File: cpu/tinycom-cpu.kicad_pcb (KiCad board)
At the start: 4 copper layers, 39.9 x 41.4 mm, 10 parts, among them P1 CONN_02X08, P2 CONN_02X08, U1 OLIMEX_IC_A13, U2 H5TQG63BFR/FBGA96, Y1 Crystal

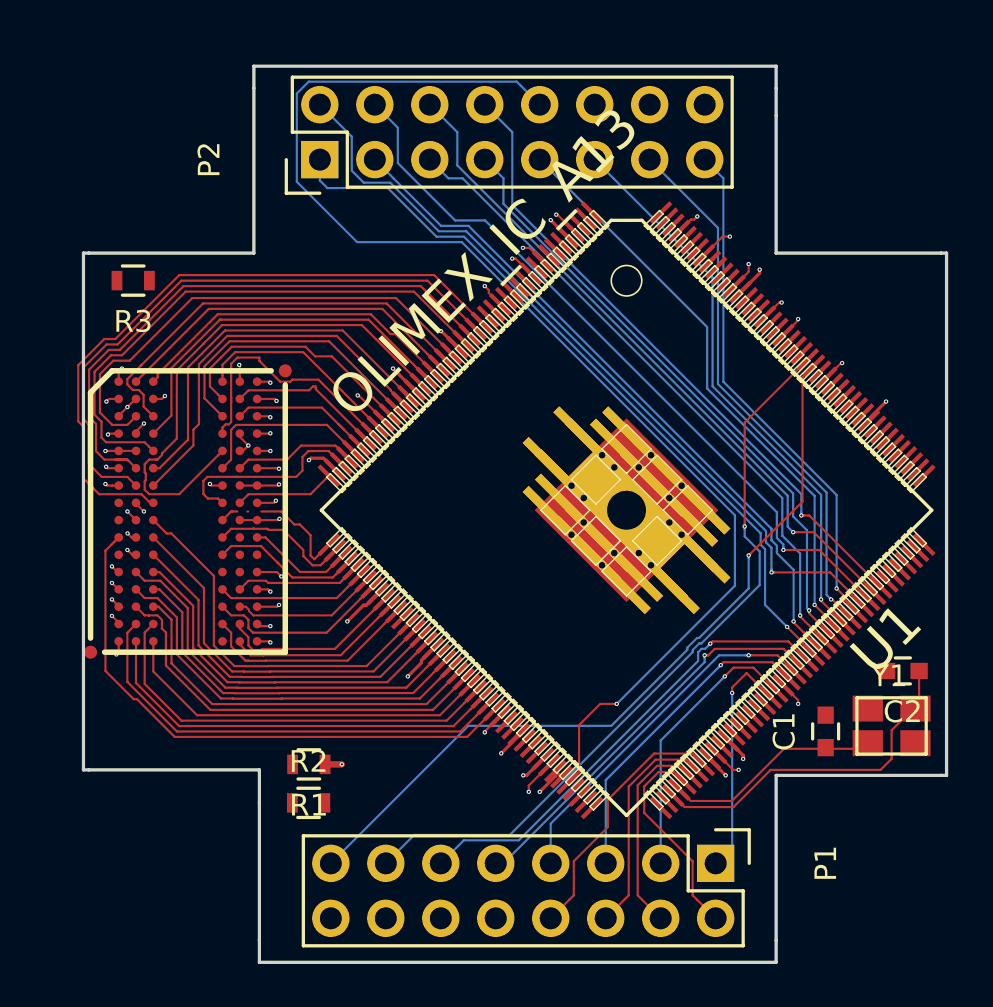
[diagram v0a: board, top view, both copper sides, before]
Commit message: change ddr to bga78
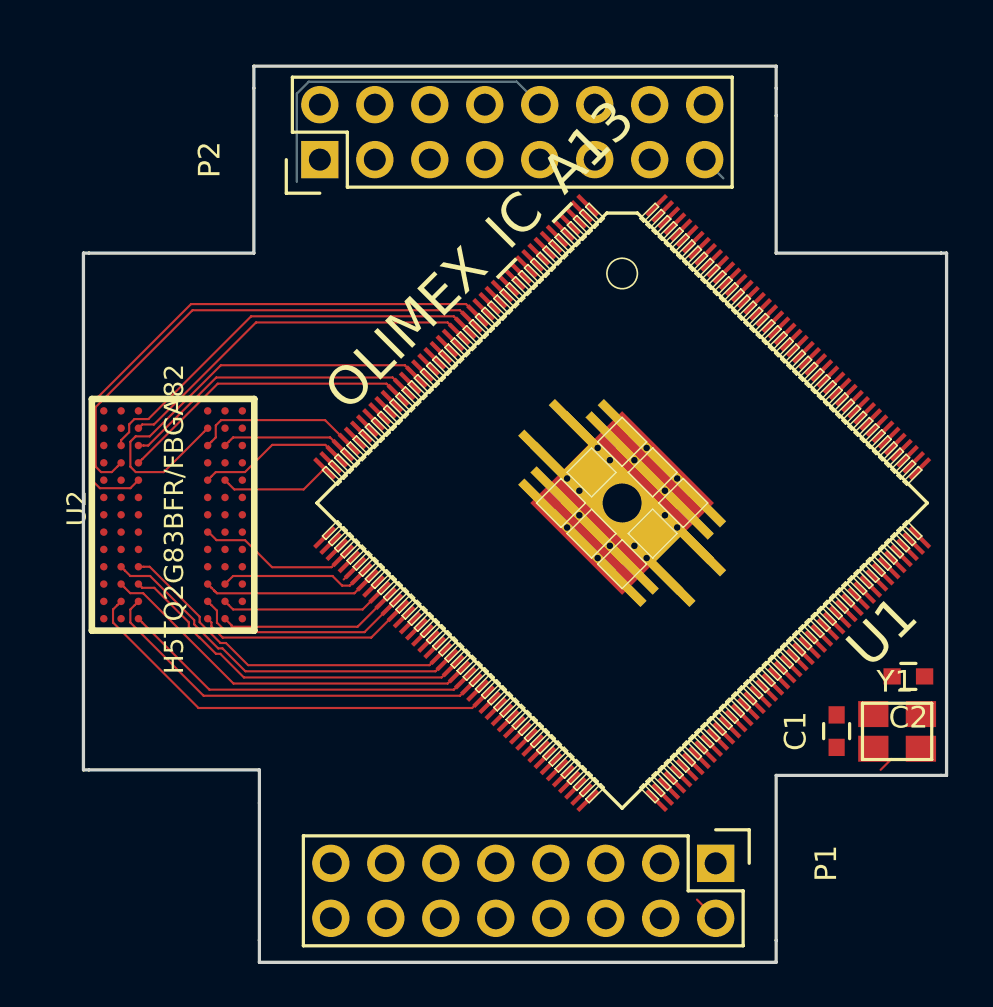
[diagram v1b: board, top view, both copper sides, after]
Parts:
- removed R1, R2, R3: R, Resistors_SMD:R_0603
- U1: footprint allwinner_a13-OLIMEX_IC_TQFP176 -> A13o:allwinner_a13-OLIMEX_IC_TQFP176
- U2: value H5TQG63BFR/FBGA96 -> H5TQ2G83BFR/FBGA82; footprint ax209:ax209-OLIMEX_IC_FBGA96 -> BGA78:BGA78
- moved U2 6.06 mm to (79.4, 106.3)
- moved C1 0.51 mm to (113.3, 121.1)
- moved U1 0.39 mm to (103.4, 110.6)
- moved Y1 0.36 mm to (116.1, 121.2)
- moved C2 0.36 mm to (116.6, 118.6)
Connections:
- U1 pad 19: DDR_D4 -> DDR3_D4
- U1 pad 20: DDR_D6 -> DDR3_D6
- U1 pad 21: DDR_D2 -> DDR3_D2
- U1 pad 22: DDR_D0 -> DDR3_D0
- U1 pad 24: DDR_D11 -> DDR3_D11
- U1 pad 25: DDR_D9 -> DDR3_D9
- U1 pad 26: DDR_D13 -> DDR3_D13
- U1 pad 27: DDR_D15 -> DDR3_D15
- U1 pad 28: DDR_DQM1 -> DDR3_DM1
- U1 pad 29: DDR_DQM0 -> DDR3_DM0
- U1 pad 31: DDR_DQS0_P -> DDR3_DQS0_P
- U1 pad 32: DDR_DQS0_N -> DDR3_DQS0_N
- U1 pad 33: DDR_DQS1_P -> DDR3_DQS1_P
- U1 pad 34: DDR_DQS1_N -> DDR3_DQS1_N
- U1 pad 36: DDR_D12 -> DDR3_D12
- U1 pad 37: DDR_D8 -> DDR3_D8
- U1 pad 38: DDR_D14 -> DDR3_D14
- U1 pad 39: DDR_D10 -> DDR3_D10
- U1 pad 40: DDR_D1 -> DDR3_D1
- U1 pad 41: DDR_D3 -> DDR3_D3
- U1 pad 42: DDR_D7 -> DDR3_D7
- U1 pad 44: DDR_D5 -> DDR3_D5
- U1 pad 48: DDR_A10 -> DDR3_A10
- U1 pad 50: DDR_A12 -> DDR3_A12
- U1 pad 51: DDR_A4 -> DDR3_A4
- U1 pad 52: DDR_A1 -> DDR3_A1
- U1 pad 54: DDR_A6 -> DDR3_A6
- U1 pad 55: DDR_A8 -> DDR3_A8
- U1 pad 56: DDR_A11 -> DDR3_A11
- U1 pad 57: DDR_A14 -> DDR3_A14
- U1 pad 64: DDR_A0 -> DDR3_A0
- U1 pad 65: DDR_A3 -> DDR3_A3
- U1 pad 66: DDR_A2 -> DDR3_A2
- U1 pad 67: DDR_A5 -> DDR3_A5
- U1 pad 68: DDR_A13 -> DDR3_A13
- U1 pad 69: DDR_A9 -> DDR3_A9
- U1 pad 71: DDR_A7 -> DDR3_A7
- U1 pad 72: DDR_ODT -> DDR3_ODT
- U2 pad A1: VCC_15 -> Net-(U2-PadA1)
- U2 pad A2: DDR_D13 -> Net-(U2-PadA2)
- U2 pad A3: DDR_D15 -> Net-(U2-PadA3)
- U2 pad A7: DDR_D12 -> Net-(U2-PadA7)
- U2 pad A8: VCC_15 -> Net-(U2-PadA8)
- U2 pad A9: GND -> Net-(U2-PadA9)
- U2 pad B1: GND -> Net-(U2-PadB1)
- U2 pad B2: VCC_15 -> Net-(U2-PadB2)
- U2 pad B3: GND -> DDR3_D0
- U2 pad B7: DDR_DQS1_N -> DDR3_DM0
- U2 pad B8: DDR_D14 -> Net-(U2-PadB8)
- U2 pad B9: GND -> Net-(U2-PadB9)
- U2 pad C1: VCC_15 -> Net-(U2-PadC1)
- U2 pad C2: DDR_D11 -> DDR3_D2
- U2 pad C3: DDR_D9 -> DDR3_DQS0_P
- U2 pad C7: DDR_DQS1_P -> DDR3_D1
- U2 pad C8: DDR_D10 -> DDR3_D3
- U2 pad C9: VCC_15 -> Net-(U2-PadC9)
- U2 pad D1: GND -> Net-(U2-PadD1)
- U2 pad D2: VCC_15 -> DDR3_D6
- U2 pad D3: DDR_DQM1 -> DDR3_DQS0_N
- U2 pad D7: DDR_D8 -> Net-(U2-PadD7)
- U2 pad D8: GND -> Net-(U2-PadD8)
- U2 pad D9: VCC_15 -> Net-(U2-PadD9)
- U2 pad E1: GND -> Net-(U2-PadE1)
- U2 pad E2: GND -> Net-(U2-PadE2)
- U2 pad E3: DDR_D0 -> DDR3_D4
- U2 pad E7: DDR_DQM0 -> DDR3_D7
- U2 pad E8: GND -> DDR3_D5
- U2 pad E9: VCC_15 -> Net-(U2-PadE9)
- U2 pad F1: VCC_15 -> Net-(U2-PadF1)
- U2 pad F2: DDR_D2 -> Net-(U2-PadF2)
- U2 pad F3: DDR_DQS0_P -> Net-(U2-PadF3)
- U2 pad F7: DDR_D1 -> Net-(U2-PadF7)
- U2 pad F8: DDR_D3 -> Net-(U2-PadF8)
- U2 pad F9: GND -> Net-(U2-PadF9)
- U2 pad G1: GND -> Net-(U2-PadG1)
- U2 pad G2: DDR_D6 -> Net-(U2-PadG2)
- U2 pad G3: DDR_DQS0_N -> Net-(U2-PadG3)
- U2 pad G7: VCC_15 -> Net-(U2-PadG7)
- U2 pad G8: GND -> Net-(U2-PadG8)
- U2 pad G9: GND -> Net-(U2-PadG9)
- U2 pad H1: Net-(R1-Pad2) -> Net-(U2-PadH1)
- U2 pad H2: VCC_15 -> Net-(U2-PadH2)
- U2 pad H3: DDR_D4 -> Net-(U2-PadH3)
- U2 pad H7: DDR_D7 -> DDR3_A10
- U2 pad H8: DDR_D5 -> Net-(U2-PadH8)
- U2 pad H9: VCC_15 -> Net-(U2-PadH9)
- U2 pad J2: GND -> Net-(U2-PadJ2)
- U2 pad J3: DDR_RAS_N -> Net-(U2-PadJ3)
- U2 pad J7: DDR_CK_P -> Net-(U2-PadJ7)
- U2 pad J8: GND -> Net-(U2-PadJ8)
- U2 pad J9: GND -> Net-(U2-PadJ9)
- U2 pad K1: DDR_ODT -> Net-(U2-PadK1)
- U2 pad K2: VCC_15 -> DDR3_A3
- U2 pad K3: DDR_CAS_N -> DDR3_A0
- U2 pad K7: DDR_CK_N -> DDR3_A12
- U2 pad K8: VCC_15 -> Net-(U2-PadK8)
- U2 pad K9: DDR_CKE -> Net-(U2-PadK9)
- U2 pad L2: GND -> DDR3_A5
- U2 pad L3: DDR_WE_N -> DDR3_A2
- U2 pad L7: DDR_A10 -> DDR3_A1
- U2 pad L8: Net-(R3-Pad1) -> DDR3_A4
- U2 pad M1: GND -> Net-(U2-PadM1)
- U2 pad M2: DDR_BA0 -> DDR3_A7
- U2 pad M3: DDR_BA2 -> DDR3_A9
- U2 pad M7: Net-(U2-PadM7) -> DDR3_A11
- U2 pad M8: Net-(R1-Pad2) -> DDR3_A6
- U2 pad M9: GND -> Net-(U2-PadM9)
- U2 pad N1: VCC_15 -> Net-(U2-PadN1)
- U2 pad N2: DDR_A3 -> Net-(U2-PadN2)
- U2 pad N3: DDR_A0 -> DDR3_A13
- U2 pad N7: DDR_A12 -> DDR3_A14
- U2 pad N8: DDR_BA1 -> DDR3_A8
- U2 pad N9: VCC_15 -> Net-(U2-PadN9)
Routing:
- net VCC_15: track 63.7 -> 0.00 mm, vias 22 -> 0
- net MICIN1: track 58.6 -> 16.0 mm, vias 1 -> 0
- net CSI_D4: track 36.6 -> 0.00 mm, vias 1 -> 0
- net UART1_RX: track 36.2 -> 0.00 mm, vias 1 -> 0
- net CSI_CLK: track 34.7 -> 0.00 mm, vias 1 -> 0
- net UART1_TX: track 34.6 -> 0.00 mm, vias 1 -> 0
- net CSI_D5: track 34.1 -> 0.00 mm, vias 1 -> 0
- net CSI_MCLK: track 31.9 -> 0.00 mm, vias 1 -> 0
- net CSI_D6: track 31.7 -> 0.00 mm, vias 1 -> 0
- net DDR_D4: track 30.5 -> 0.00 mm
- net CSI_HSYNC: track 30.3 -> 0.00 mm, vias 1 -> 0
- net CSI_D7: track 30.1 -> 0.00 mm, vias 1 -> 0
- net CSI_VSYNC: track 28.7 -> 0.00 mm, vias 1 -> 0
- net DDR_D6: track 27.9 -> 0.00 mm
- net CSI_D0: track 27.5 -> 0.00 mm, vias 1 -> 0
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
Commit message: route new ddr
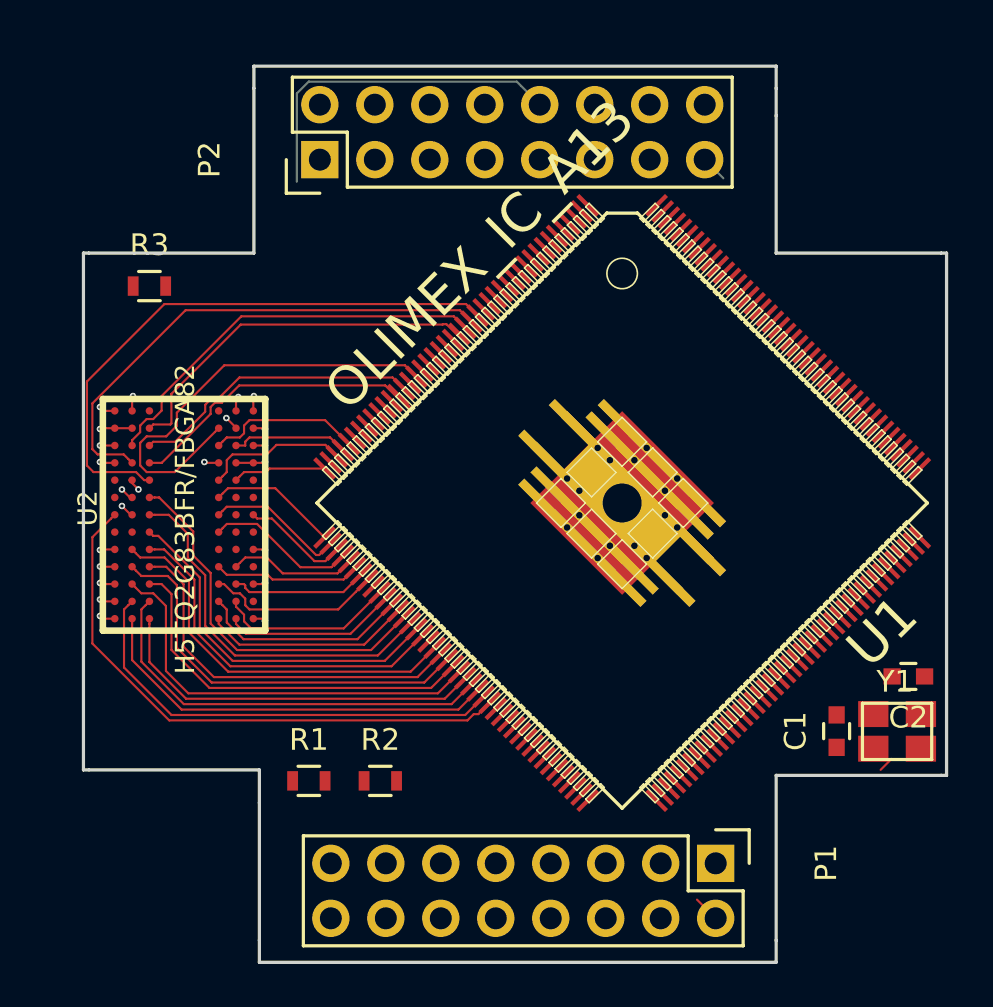
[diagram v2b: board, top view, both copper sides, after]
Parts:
- added R1: R, Resistors_SMD:R_0603, F.Cu at (88.9, 123.4)
- added R2: R, Resistors_SMD:R_0603, F.Cu at (92.2, 123.4)
- added R3: R, Resistors_SMD:R_0603, F.Cu at (81.5, 100.6)
- moved U2 0.51 mm to (79.9, 106.3)
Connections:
- U1 pad 45: DDR_CK_P -> DDR3_CK_P
- U1 pad 46: DDR_CK_N -> DDR3_CK_N
- U1 pad 47: DDR_CKE -> DDR3_CKE
- U1 pad 49: DDR_BA1 -> DDR3_BA1
- U1 pad 58: DDR_RAS_N -> DDR3_RAS_N
- U1 pad 59: DDR_CAS_N -> DDR3_CAS_N
- U1 pad 60: DDR_WE_N -> DDR3_WE_N
- U1 pad 61: DDR_BA2 -> DDR3_BA2
- U1 pad 63: DDR_BA0 -> DDR3_BA0
- U1 pad 70: DDR_RST -> DDR3_RST
- U2 pad A1: Net-(U2-PadA1) -> GND
- U2 pad A2: Net-(U2-PadA2) -> VCC_15
- U2 pad A8: Net-(U2-PadA8) -> GND
- U2 pad A9: Net-(U2-PadA9) -> VCC_15
- U2 pad B1: Net-(U2-PadB1) -> GND
- U2 pad B2: Net-(U2-PadB2) -> GND
- U2 pad B8: Net-(U2-PadB8) -> GND
- U2 pad B9: Net-(U2-PadB9) -> VCC_15
- U2 pad C1: Net-(U2-PadC1) -> VCC_15
- U2 pad C9: Net-(U2-PadC9) -> GND
- U2 pad D1: Net-(U2-PadD1) -> GND
- U2 pad D7: Net-(U2-PadD7) -> VCC_15
- U2 pad D8: Net-(U2-PadD8) -> GND
- U2 pad D9: Net-(U2-PadD9) -> GND
- U2 pad E1: Net-(U2-PadE1) -> Net-(R1-Pad2)
- U2 pad E2: Net-(U2-PadE2) -> VCC_15
- U2 pad E9: Net-(U2-PadE9) -> VCC_15
- U2 pad F2: Net-(U2-PadF2) -> GND
- U2 pad F3: Net-(U2-PadF3) -> DDR3_RAS_N
- U2 pad F7: Net-(U2-PadF7) -> DDR3_CK_P
- U2 pad F8: Net-(U2-PadF8) -> GND
- U2 pad G1: Net-(U2-PadG1) -> DDR3_ODT
- U2 pad G2: Net-(U2-PadG2) -> VCC_15
- U2 pad G3: Net-(U2-PadG3) -> DDR3_CAS_N
- U2 pad G7: Net-(U2-PadG7) -> DDR3_CK_N
- U2 pad G8: Net-(U2-PadG8) -> VCC_15
- U2 pad G9: Net-(U2-PadG9) -> DDR3_CKE
- U2 pad H2: Net-(U2-PadH2) -> GND
- U2 pad H3: Net-(U2-PadH3) -> DDR3_WE_N
- U2 pad J1: Net-(U2-PadJ1) -> GND
- U2 pad J2: Net-(U2-PadJ2) -> DDR3_BA0
- U2 pad J3: Net-(U2-PadJ3) -> DDR3_BA2
- U2 pad J8: Net-(U2-PadJ8) -> Net-(R1-Pad2)
- U2 pad J9: Net-(U2-PadJ9) -> GND
- U2 pad K1: Net-(U2-PadK1) -> VCC_15
- U2 pad K8: Net-(U2-PadK8) -> DDR3_BA1
- U2 pad K9: Net-(U2-PadK9) -> VCC_15
- U2 pad L1: Net-(U2-PadL1) -> GND
- U2 pad L9: Net-(U2-PadL9) -> GND
- U2 pad M1: Net-(U2-PadM1) -> VCC_15
- U2 pad M9: Net-(U2-PadM9) -> VCC_15
- U2 pad N1: Net-(U2-PadN1) -> GND
- U2 pad N2: Net-(U2-PadN2) -> DDR3_RST
- U2 pad N9: Net-(U2-PadN9) -> GND
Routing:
- net DDR3_ODT: track 0.00 -> 26.5 mm
- net DDR3_RST: track 0.00 -> 19.2 mm
- net DDR3_BA0: track 0.00 -> 18.2 mm
- net DDR3_CAS_N: track 0.00 -> 17.4 mm
- net DDR3_RAS_N: track 0.00 -> 17.3 mm
- net DDR3_BA2: track 0.00 -> 16.8 mm
- net DDR3_WE_N: track 0.00 -> 16.8 mm
- net GND: track 0.00 -> 10.6 mm, vias 0 -> 14
- net DDR3_CK_N: track 0.00 -> 6.47 mm
- net VCC_15: track 0.00 -> 6.04 mm, vias 0 -> 9
- net DDR3_A12: track 0.75 -> 6.77 mm
- net DDR3_CK_P: track 0.00 -> 6.01 mm
- net DDR3_BA1: track 0.00 -> 5.92 mm
- net DDR3_CKE: track 0.00 -> 4.96 mm
- net DDR3_A5: track 17.7 -> 19.4 mm
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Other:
- net class Default: via_dia 0.2 -> 0.3; via_drill 0.1 -> 0.15
- net class ddr_address removed
- net class ddr_byte_0 removed
- net class ddr_byte_1 removed
- net class ddr_clock removed
- net class ddr_control removed
- net class vcc_15 removed
- net class vcc_33 removed

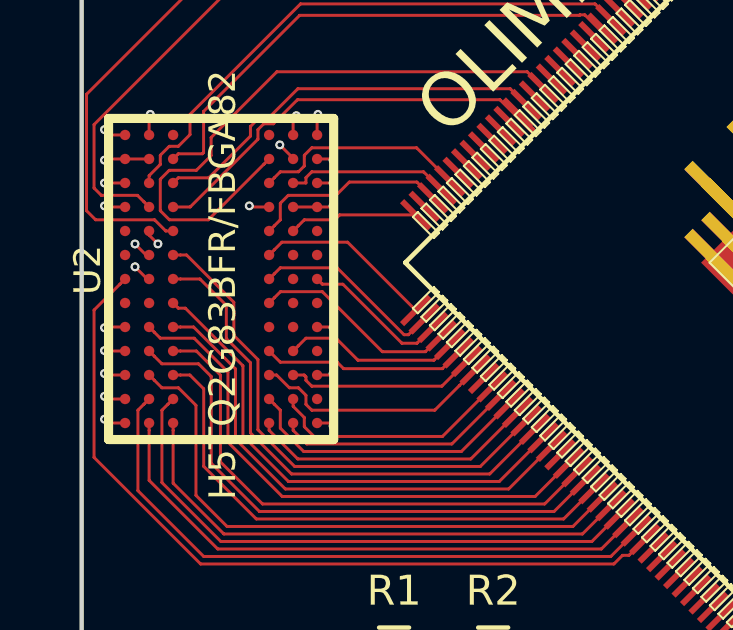
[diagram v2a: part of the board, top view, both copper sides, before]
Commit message: add ddr power plane
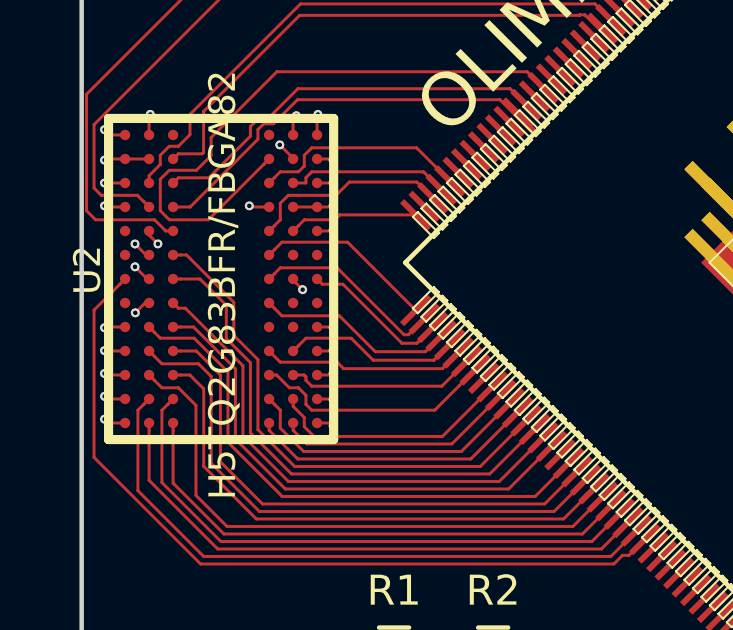
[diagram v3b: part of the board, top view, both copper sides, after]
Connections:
- P1 pad 12: VCC_15 -> VCC_33
- P1 pad 14: VCC_30 -> VCC_15
- P1 pad 16: VCC_33 -> GND
- P2 pad 14: GND -> VCC_30
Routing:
- net VCC_15: track 6.04 -> 76.7 mm, vias 9 -> 13
- net VCC_33: track 6.22 -> 0.00 mm
- net GND: track 10.6 -> 11.2 mm, vias 14 -> 15
- added copper zone on In2.Cu, net VCC_15

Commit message: router power
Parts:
- moved C2 4.38 mm to (113.0, 121.2), turned to 90 degrees
- moved C1 3.95 mm to (116.3, 118.6), turned to 180 degrees
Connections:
- P1 pad 1: SDC0_D1 -> SDC0_D2
- P1 pad 11: SDC0_D2 -> SDC0_D1
- P1 pad 13: UART1_TX -> UART1_RX
- P1 pad 15: UART1_RX -> UART1_TX
- P1 pad 3: SDC0_D0 -> SDC0_D3
- P1 pad 5: SDC0_CLK -> SDC0_CMD
- P1 pad 7: SDC0_CMD -> SDC0_CLK
- P1 pad 9: SDC0_D3 -> SDC0_D0
- Y1 pad 1: Net-(C1-Pad1) -> Net-(C2-Pad1)
- Y1 pad 2: Net-(C2-Pad1) -> Net-(C1-Pad1)
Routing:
- net VCC_14: track 0.00 -> 112.2 mm, vias 0 -> 13
- net VCC_33: track 0.00 -> 83.1 mm, vias 0 -> 8
- net CSI_D4: track 0.00 -> 37.4 mm, vias 0 -> 1
- net UART1_TX: track 0.00 -> 36.9 mm, vias 0 -> 1
- net MICIN1: track 16.0 -> 52.4 mm, vias 0 -> 1
- net CSI_D5: track 0.00 -> 36.1 mm, vias 0 -> 1
- net UART1_RX: track 0.00 -> 35.6 mm, vias 0 -> 1
- net CSI_CLK: track 0.00 -> 35.5 mm, vias 0 -> 1
- net CSI_MCLK: track 0.00 -> 32.8 mm, vias 0 -> 1
- net CSI_D6: track 0.00 -> 31.7 mm, vias 0 -> 1
- net CSI_HSYNC: track 0.00 -> 30.5 mm, vias 0 -> 1
- net CSI_D7: track 0.00 -> 30.2 mm, vias 0 -> 1
- net CSI_VSYNC: track 0.00 -> 28.8 mm, vias 0 -> 1
- net CSI_D0: track 0.00 -> 27.7 mm, vias 0 -> 1
- net CSI_D1: track 0.00 -> 25.8 mm, vias 0 -> 1
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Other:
- net class Default: trace_width 0.1 -> 0.15
- net class power added: clearance 0.15, trace_width 0.3, via_dia 0.3, via_drill 0.15
